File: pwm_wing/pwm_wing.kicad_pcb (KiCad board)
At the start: 2 copper layers, 47 x 49.5 mm, 13 parts, among them P1 CONN_4X2, P2 CONN_2, P3 CONN_6, U1 VN9205-e, U2 VN9205-e, U3 VN9205-e

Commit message: clean
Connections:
- P1 pad 6: GND -> (no net)

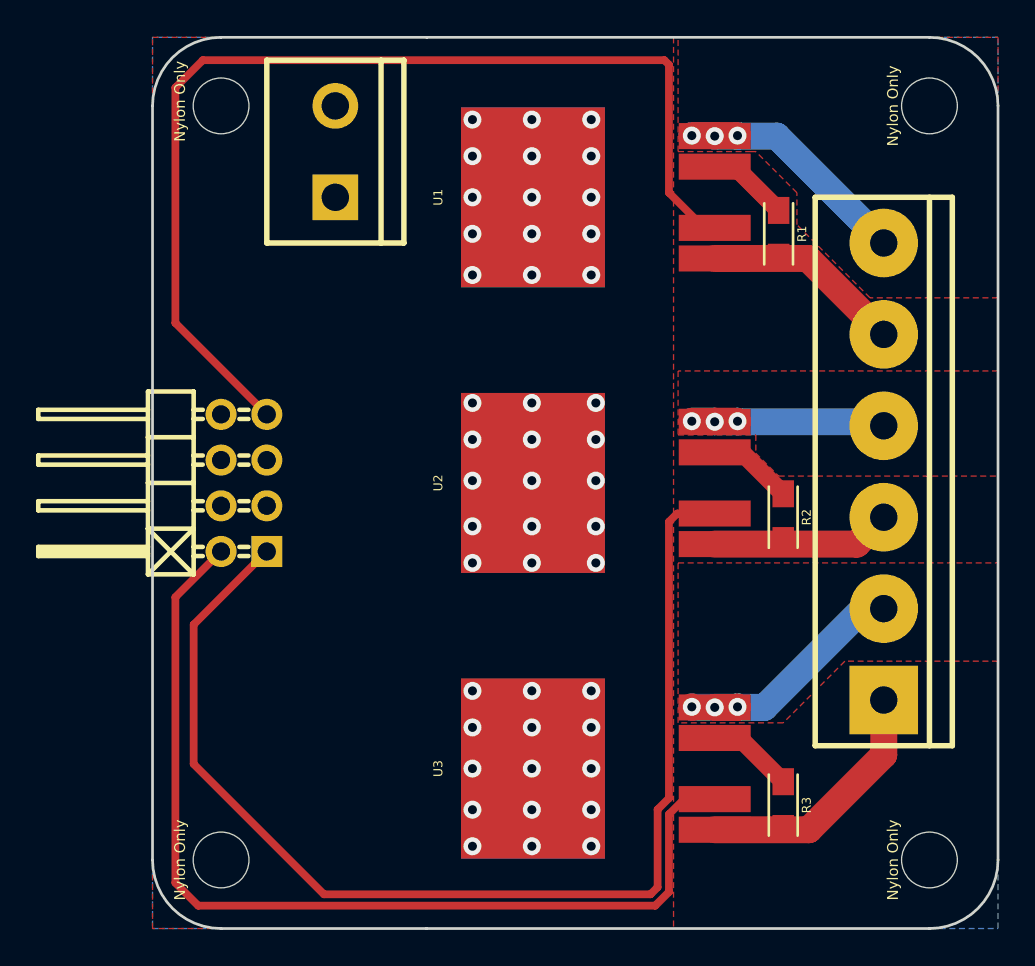
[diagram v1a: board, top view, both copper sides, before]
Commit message: need to enbigen silk
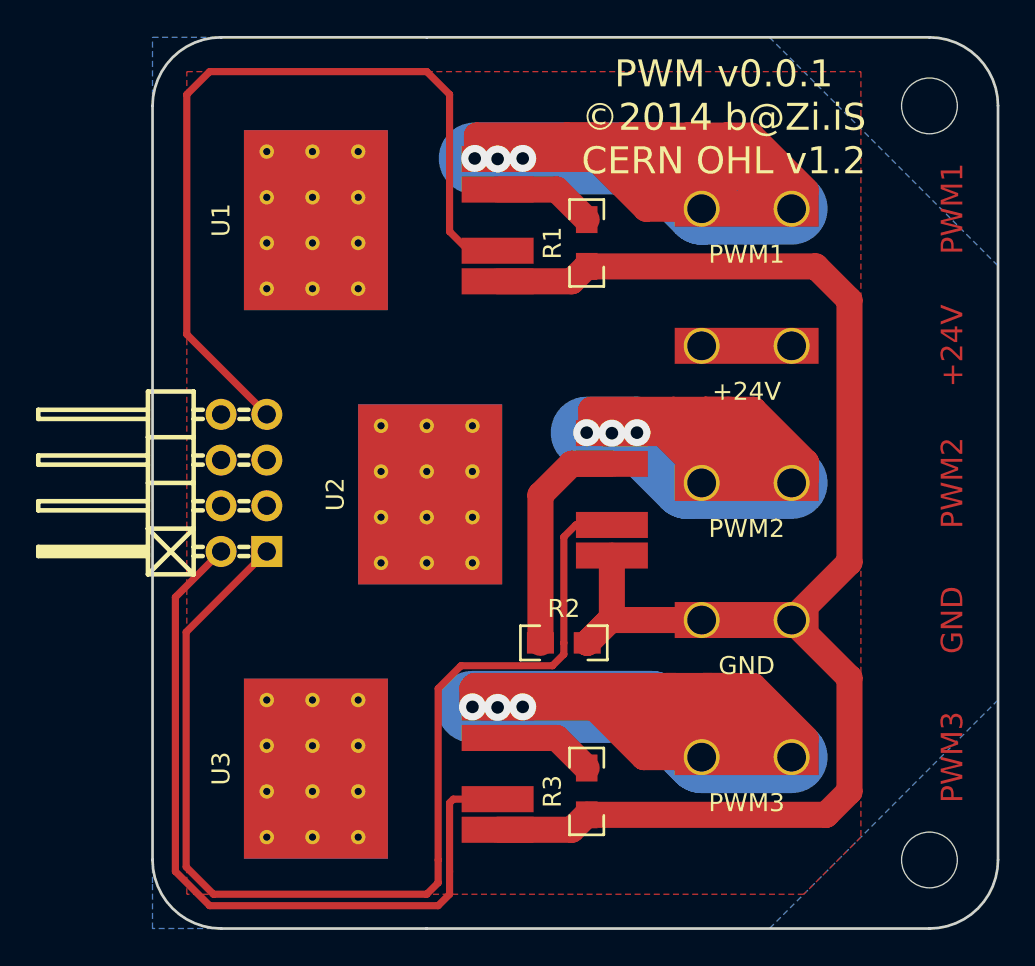
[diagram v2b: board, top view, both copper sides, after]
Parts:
- removed the Nylon Only at (106.4, 80.5)
- removed the Nylon Only at (106.4, 122.4)
- removed P2: CONN_2, Connect:bornier2
- added P4: PWM1, Local:TabRA, F.Cu at (135.6, 86.2)
- added P5: PWM2, Local:TabRA, F.Cu at (135.6, 101.5)
- added P6: PWM3, Local:TabRA, F.Cu at (135.6, 116.7)
- added eP2: GND, Local:TabRA, F.Cu at (135.6, 109.1)
- P1: value CONN_4X2 -> +24V; footprint Pin_Headers:Pin_Header_Angled_2x04 -> Local:TabRA
- P3: value CONN_6 -> CONN_4X2; footprint Connect:bornier6 -> Pin_Headers:Pin_Header_Angled_2x04
- R1, R2, R3: footprint Resistors_SMD:R_0805_HandSoldering -> Local:0805R
- moved P3 35.6 mm to (107.7, 101.5)
- moved P1 29.0 mm to (135.6, 93.9), turned to 0 degrees
- moved R2 14.1 mm to (125.5, 110.4), turned to 0 degrees
- moved U1 12.1 mm to (107.7, 86.9)
- moved U3 12.1 mm to (107.7, 117.3)
- moved R3 10.9 mm to (126.7, 118.6)
- moved R1 10.7 mm to (126.7, 88.1)
- moved U2 5.75 mm to (114.0, 102.1)
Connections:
- P1 pad 1: /PWM1 -> +24V
- P3 pad 1: GND -> /PWM1
- P3 pad 2: Net-(P3-Pad2) -> /PWM2
- P3 pad 3: GND -> (no net)
- P3 pad 4: Net-(P3-Pad4) -> (no net)
- P3 pad 5: GND -> (no net)
- P3 pad 6: Net-(P3-Pad6) -> (no net)
- U1 pad 5: Net-(P3-Pad6) -> Net-(P4-Pad1)
- U2 pad 5: Net-(P3-Pad4) -> Net-(P5-Pad1)
- U3 pad 5: Net-(P3-Pad2) -> Net-(P6-Pad1)
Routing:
- net +24V: track 146.6 -> 0.00 mm, vias 45 -> 0
- net Net-(P6-Pad1): track 0.00 -> 98.5 mm, vias 0 -> 3
- net Net-(P4-Pad1): track 0.00 -> 95.5 mm, vias 0 -> 3
- net Net-(P5-Pad1): track 0.00 -> 69.8 mm, vias 0 -> 3
- net GND: track 59.4 -> 88.4 mm
- net Net-(P3-Pad6): track 15.8 -> 0.00 mm, vias 3 -> 0
- net Net-(P3-Pad2): track 14.4 -> 0.00 mm, vias 3 -> 0
- net Net-(P3-Pad4): track 13.4 -> 0.00 mm, vias 3 -> 0
- net /PWM0: track 58.9 -> 46.0 mm
- net /PWM2: track 54.9 -> 43.0 mm
- net Net-(R2-Pad1): track 4.76 -> 12.9 mm
- net /PWM1: track 67.6 -> 62.3 mm
- net Net-(R1-Pad1): track 4.56 -> 5.64 mm
- net Net-(R3-Pad1): track 4.81 -> 5.64 mm
- added copper zone on B.Cu, net +24V
- removed copper zone on B.Cu, net GND
- removed copper zone on F.Cu, net Net-(P3-Pad2)
- removed copper zone on F.Cu, net Net-(P3-Pad4)
- removed copper zone on F.Cu, net Net-(P3-Pad6)
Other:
- net class Default: clearance 0.2 -> 0.4; trace_width 0.4318 -> 0.4; via_dia 1 -> 1.5; via_drill 0.5 -> 0.7
- rule pad_to_mask_clearance: 0.2 -> 0
- rule trace_clearance: 0.2 -> 0.4
- board text added: "+24V"
- board text added: "GND"
- board text added: "PWM v0.0.1 ©2014 b@Zi.iS CERN OHL v1.2"
- board text added: "PWM1"
- board text added: "PWM2"
- board text added: "PWM3"

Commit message: more titdy
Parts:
- removed Nylon Only: 3-1mm, Local:MountingHole_3-1mm (x2)
- removed eP2: GND, Local:TabRA
- added M1: GND, Local:MountingHole_3-1mm, F.Cu at (145.8, 122.4)
- added M2: GND, Local:MountingHole_3-1mm, F.Cu at (145.8, 80.5)
- added P2: GND, Local:TabRA, F.Cu at (135.6, 109.1)
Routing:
- net GND: track 88.4 -> 102.0 mm
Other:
- net class Default: via_dia 1.5 -> 1.2; via_drill 0.7 -> 0.4
